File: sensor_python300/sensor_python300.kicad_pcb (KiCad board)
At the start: 4 copper layers, 30 x 30 mm, 83 parts, among them J101 DF40HC(4.0)-60DS-0.4V(51), U101 NOIP1SN0300A-QTI, U102 TPS7A2033PDBVR, U103 TPS22918DBVR, U104 TPS7A2033PDBVR, U105 APX803S-29SA-7, U106 TPS610995DRVR, X101 <DNP> DSC1103DI5-360.0000

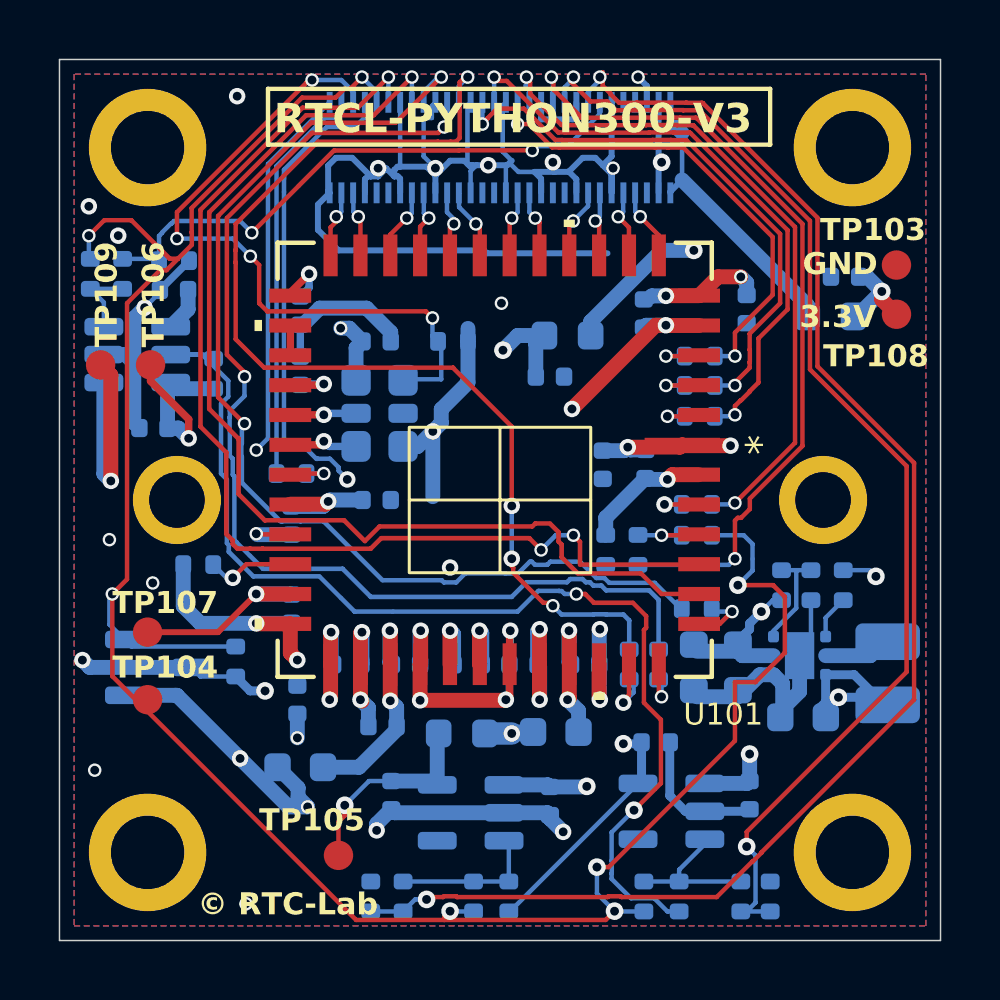
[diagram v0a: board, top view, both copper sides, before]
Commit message: KiCAD 10.0 へ
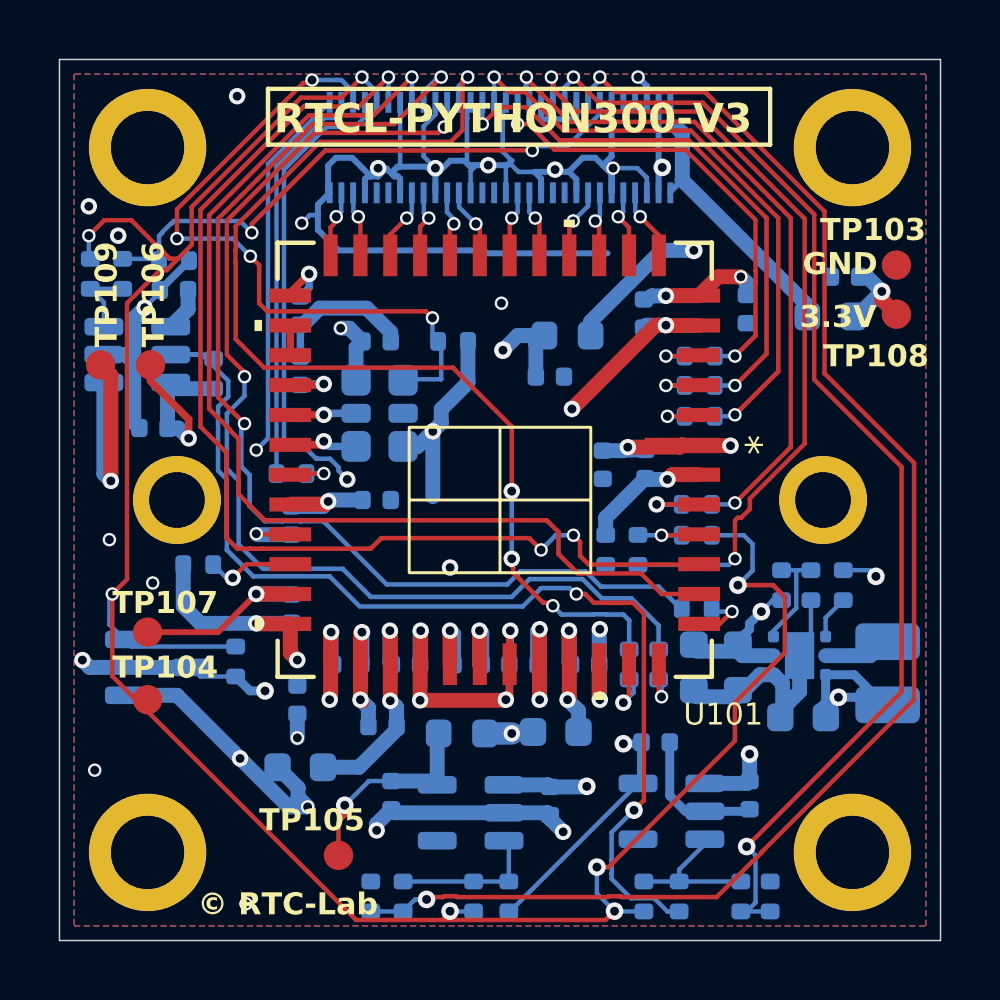
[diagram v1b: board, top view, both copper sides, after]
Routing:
- net GND: track 313.8 -> 315.3 mm, vias 38 -> 39
- net /MONITOR0: track 37.7 -> 37.2 mm
- net Net-(U101-ss_n): track 1.77 -> 2.30 mm
- net /PGOOD_VDD18: track 38.3 -> 37.7 mm
